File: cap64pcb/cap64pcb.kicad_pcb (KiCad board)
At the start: 2 copper layers, 96 x 8 mm, 29 parts, among them J1 SM05B_SURS_TF, Q1 BSS138, Q2 BSS138, U1 MPR121QR2, U2 SPX3819M5-L-3-3

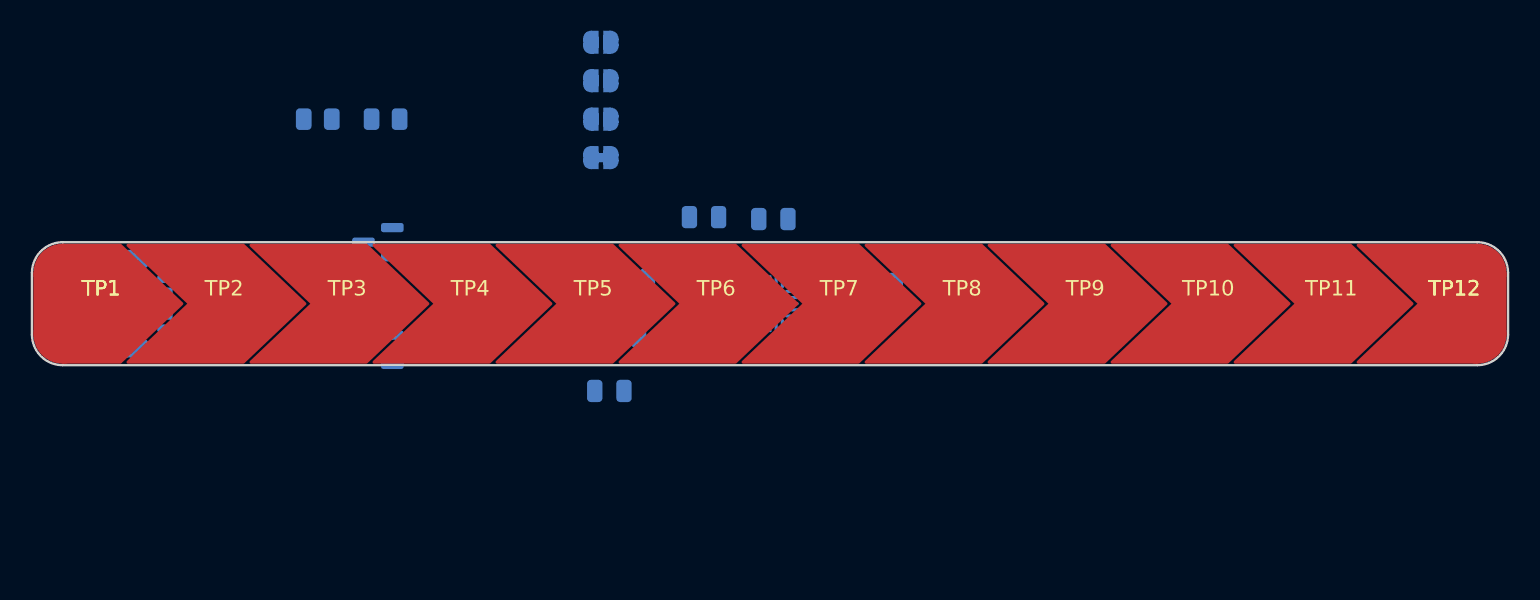
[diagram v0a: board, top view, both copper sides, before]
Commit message: reworked chevrons (merged pads, shrunk to 7.6)
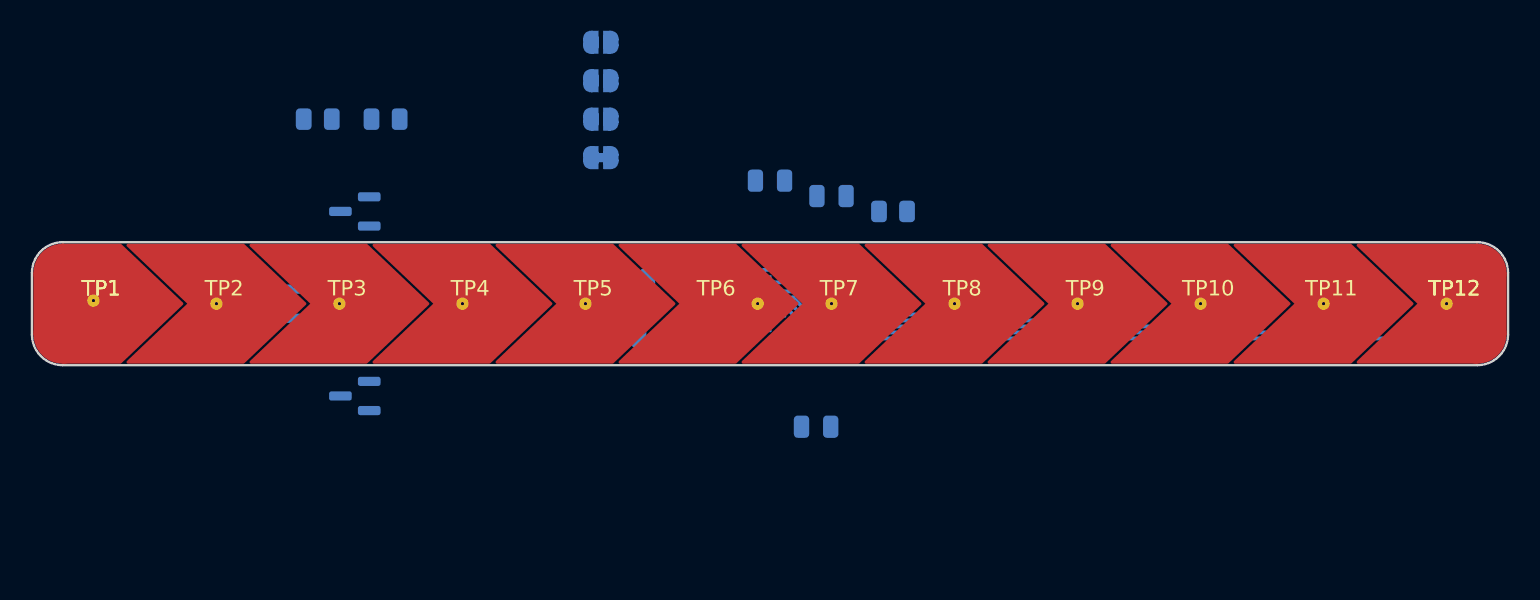
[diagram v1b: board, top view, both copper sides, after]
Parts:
- TP6: footprint cap_pads:CAPPAD_8x8_Chevron_2 -> cap_pads:CAPPAD_8x8_Chevron_2_asym
- moved C5 13.6 mm to (83.0, 53.0)
- moved C2 4.90 mm to (80.0, 37.0)
- moved R1 4.75 mm to (88.0, 39.0)
- moved C1 4.07 mm to (84.0, 38.0)
- moved Q1 3.35 mm to (53.0, 51.0)
- moved U2 3.00 mm to (48.0, 45.0)
- moved Q2 2.50 mm to (53.0, 39.0)
- moved U1 0.80 mm to (79.2, 45.0)
- moved J1 0.50 mm to (40.0, 45.0), turned to -90 degrees
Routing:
- net Net-(U1-Pad19): track 0.00 -> 45.0 mm
- net Net-(U1-Pad18): track 0.00 -> 36.9 mm
- net Net-(U1-Pad17): track 0.00 -> 28.7 mm
- net Net-(U1-Pad16): track 0.00 -> 20.6 mm
- net Net-(U1-Pad15): track 0.00 -> 13.1 mm
- net Net-(U1-Pad14): track 0.00 -> 6.12 mm
- net Net-(U1-Pad13): track 0.00 -> 1.39 mm

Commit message: fixed miniscule spacing error
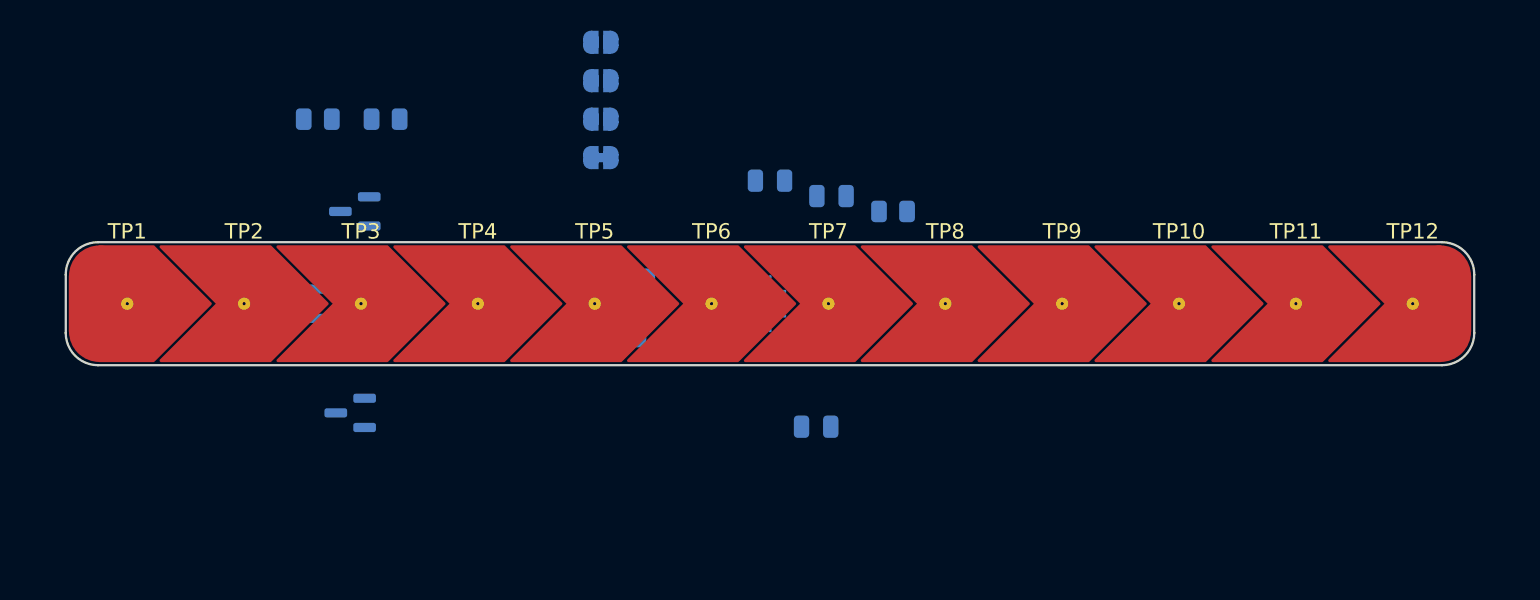
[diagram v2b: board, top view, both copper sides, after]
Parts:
- TP1: footprint cap_pads:CAPPAD_8x8_Chevron_1 -> cap_pads:CAPPAD_7.6x7.6_Chevron_1
- TP10, TP11, TP2, TP3, TP4, TP5, TP7, TP8, TP9: footprint cap_pads:CAPPAD_8x8_Chevron_2 -> cap_pads:CAPPAD_7.6x7.6_Chevron_2
- TP12: footprint cap_pads:CAPPAD_8x8_Chevron_3 -> cap_pads:CAPPAD_7.6x7.6_Chevron_3
- TP6: footprint cap_pads:CAPPAD_8x8_Chevron_2_asym -> cap_pads:CAPPAD_7.6x7.6_Chevron_2
- moved TP1 2.20 mm to (38.2, 45.0)
- moved TP12 2.20 mm to (121.8, 45.0)
- moved J1 2.10 mm to (42.1, 45.0)
- moved TP11 1.80 mm to (114.2, 45.0)
- moved TP2 1.80 mm to (45.8, 45.0)
- moved U2 1.50 mm to (49.5, 45.0)
- moved TP10 1.40 mm to (106.6, 45.0)
- moved TP3 1.40 mm to (53.4, 45.0)
- moved Q1 1.14 mm to (52.7, 52.1)
- moved TP4 1.00 mm to (61.0, 45.0)
- moved TP9 1.00 mm to (99.0, 45.0)
- moved TP5 0.60 mm to (68.6, 45.0)
- moved TP8 0.60 mm to (91.4, 45.0)
- moved TP6 0.20 mm to (76.2, 45.0)
- moved TP7 0.20 mm to (83.8, 45.0)
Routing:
- net Net-(U1-Pad19): track 45.0 -> 0.00 mm
- net Net-(U1-Pad18): track 36.9 -> 0.00 mm
- net Net-(U1-Pad17): track 28.7 -> 0.00 mm
- net Net-(U1-Pad16): track 20.6 -> 0.00 mm
- net Net-(U1-Pad15): track 13.1 -> 0.00 mm
- net Net-(U1-Pad14): track 6.12 -> 0.00 mm
- net Net-(U1-Pad13): track 1.39 -> 0.00 mm
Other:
- board size 96 x 8 mm -> 91.6 x 8 mm

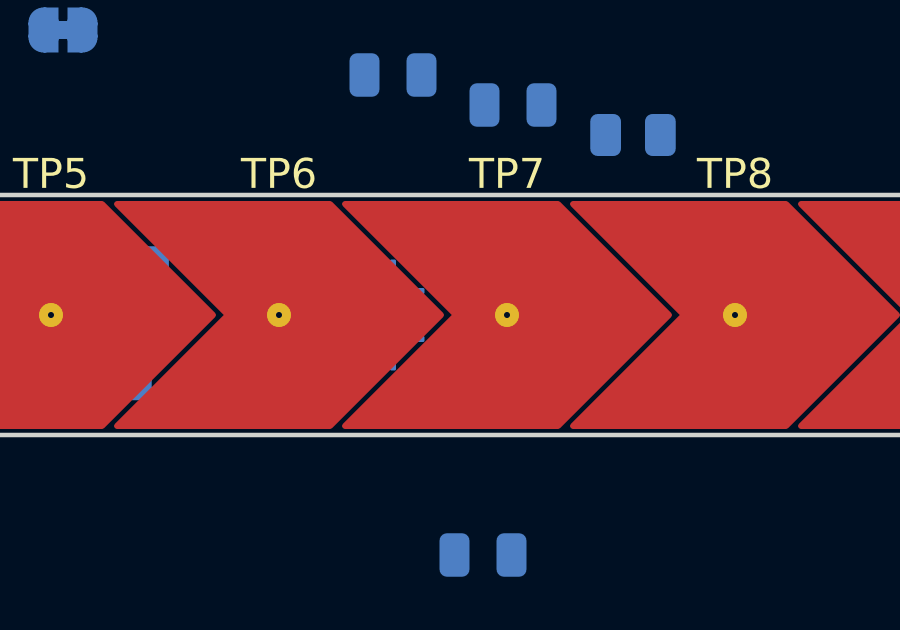
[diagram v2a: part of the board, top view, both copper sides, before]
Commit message: shifted 'via' for center pads
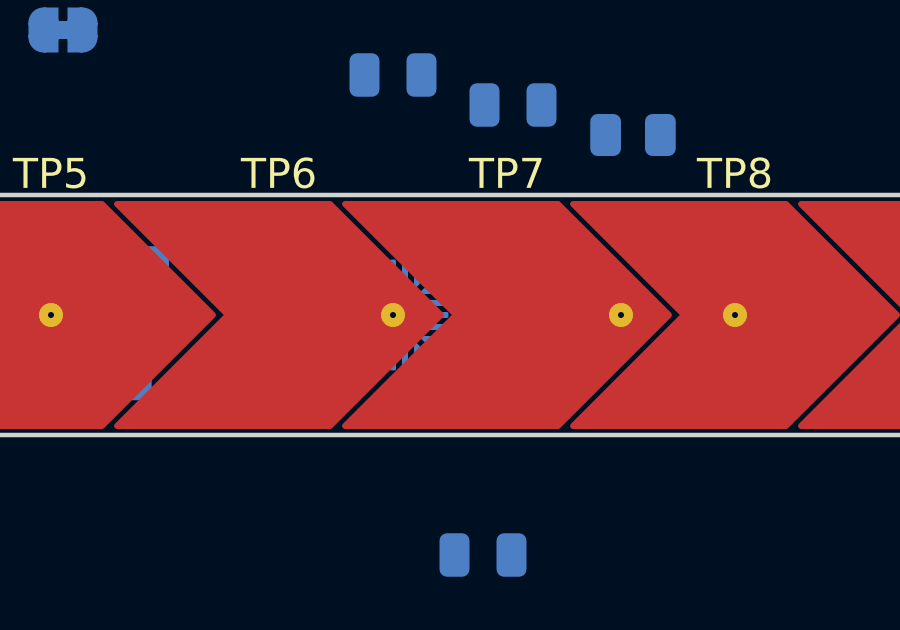
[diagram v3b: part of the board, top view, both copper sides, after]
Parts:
- TP6, TP7: footprint cap_pads:CAPPAD_7.6x7.6_Chevron_2 -> cap_pads:CAPPAD_7.6x7.6_Chevron_2_shifted
- moved U1 0.80 mm to (80.0, 45.0)
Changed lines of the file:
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@@
       (net 23 "Net-(U1-Pad18)") (pinfunction "1") (pintype "passive"))
   )
-  (footprint "cap_pads:CAPPAD_7.6x7.6_Chevron_2" (layer "F.Cu")
+  (footprint "cap_pads:CAPPAD_7.6x7.6_Chevron_2_shifted" (layer "F.Cu")
     (at 83.8 45)
     (property "Sheetfile" "cap64pcb.kicad_sch")
@@
     )
     (fp_rect (start -3.8 -3.8) (end 3.8 3.8) (layer "Dwgs.User") (width 0.1) (fill none))
+    (pad "1" thru_hole circle (at 3.8 0) (size 0.8 0.8) (drill 0.2) (layers *.Cu)
+      (net 19 "Net-(U1-Pad14)") (pinfunction "1") (pintype "passive"))
     (pad "1" smd custom (at 0 0) (size 0.8 0.8) (layers "F.Cu")
       (net 19 "Net-(U1-Pad14)") (pinfunction "1") (pintype "passive")
@@
           ) (width 0.2) (fill yes))
       ))
-    (pad "1" thru_hole circle (at 0 0) (size 0.8 0.8) (drill 0.2) (layers *.Cu)
-      (net 19 "Net-(U1-Pad14)") (pinfunction "1") (pintype "passive"))
   )
   (footprint "cap_pads:CAPPAD_7.6x7.6_Chevron_2" (layer "F.Cu")
@@
       ))
   )
-  (footprint "cap_pads:CAPPAD_7.6x7.6_Chevron_2" (layer "F.Cu")
+  (footprint "cap_pads:CAPPAD_7.6x7.6_Chevron_2_shifted" (layer "F.Cu")
     (at 76.2 45)
     (property "Sheetfile" "cap64pcb.kicad_sch")
@@
           ) (width 0.2) (fill yes))
       ))
-    (pad "1" thru_hole circle (at 0 0) (size 0.8 0.8) (drill 0.2) (layers *.Cu)
+    (pad "1" thru_hole circle (at 3.8 0) (size 0.8 0.8) (drill 0.2) (layers *.Cu)
       (net 18 "Net-(U1-Pad13)") (pinfunction "1") (pintype "passive"))
   )
@@
   )
   (footprint "Package_DFN_QFN:UQFN-20_3x3mm_P0.4mm" (layer "B.Cu")
-    (at 79.2 45 90)
+    (at 80 45 90)
     (descr "UQFN, 20 Pin (https://resurgentsemi.com/wp-content/uploads/2018/09/MPR121_rev5-Resurgent.pdf?d453f8&d453f8), generated with kicad-footprint-generator ipc_noLead_generator.py")
     (tags "UQFN NoLead")

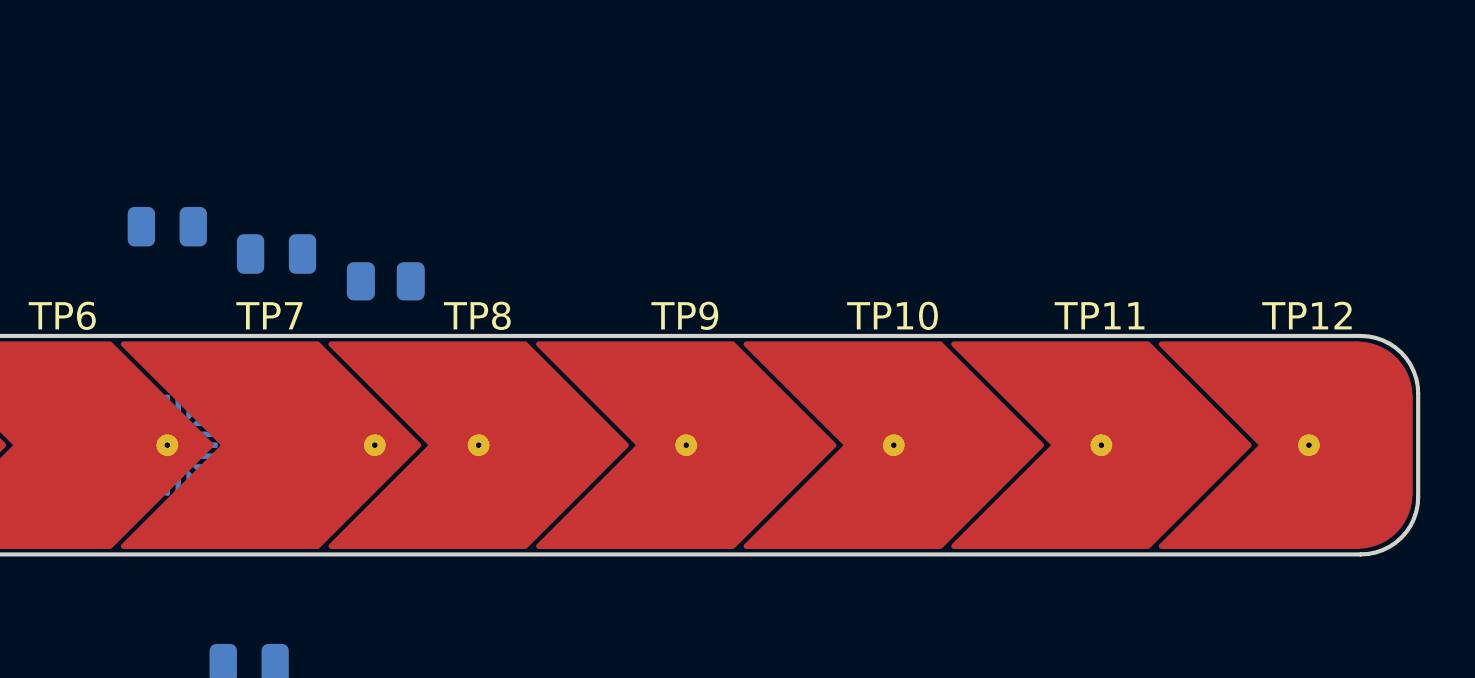
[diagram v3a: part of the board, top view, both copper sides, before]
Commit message: routed pads 7-12
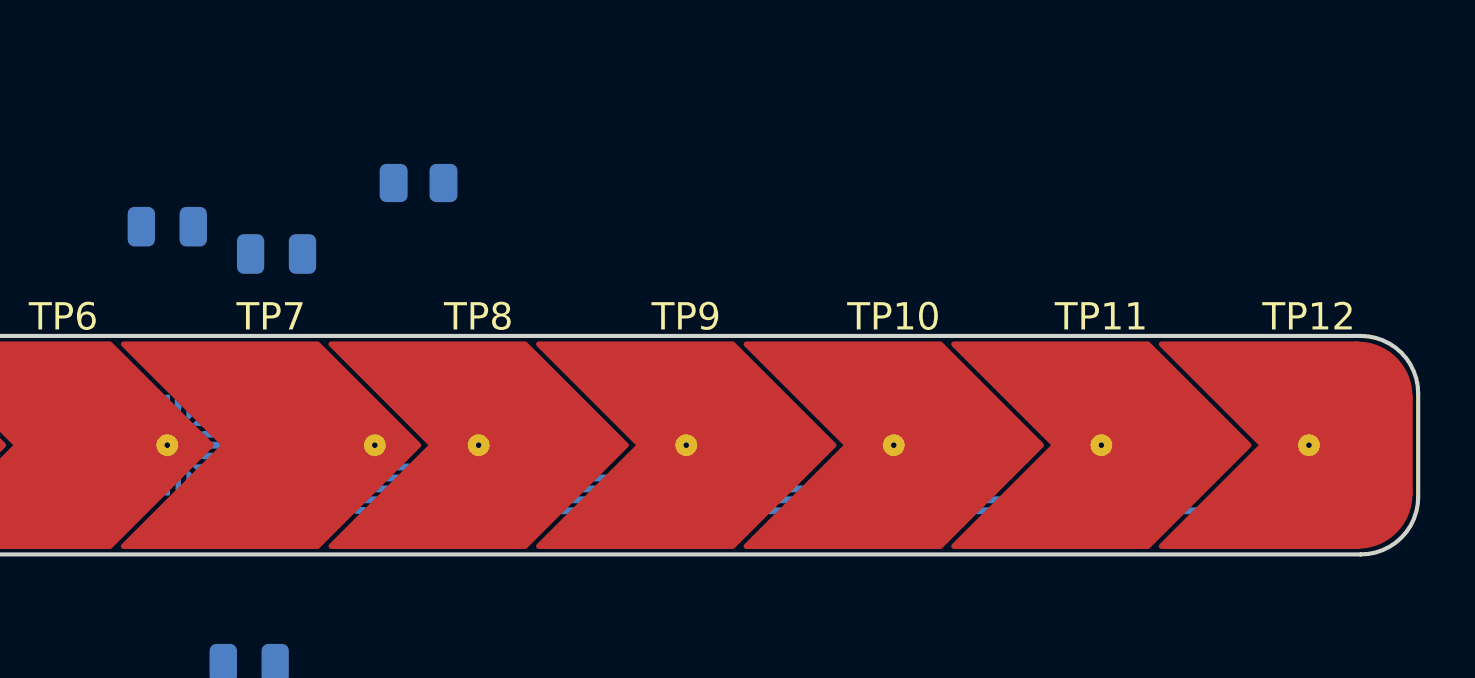
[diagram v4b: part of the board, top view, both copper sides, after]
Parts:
- moved R1 3.79 mm to (89.2, 35.4)
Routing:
- net Net-(U1-Pad19): track 0.00 -> 42.0 mm
- net Net-(U1-Pad18): track 0.00 -> 34.3 mm
- net Net-(U1-Pad17): track 0.00 -> 26.5 mm
- net Net-(U1-Pad16): track 0.00 -> 18.7 mm
- net Net-(U1-Pad15): track 0.00 -> 11.7 mm
- net Net-(U1-Pad14): track 0.00 -> 8.60 mm
- net Net-(U1-Pad13): track 0.00 -> 1.39 mm
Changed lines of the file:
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@@
   )
   (footprint "Resistor_SMD:R_0805_2012Metric" (layer "B.Cu")
-    (at 88 39 180)
+    (at 89.2 35.4 180)
     (descr "Resistor SMD 0805 (2012 Metric), square (rectangular) end terminal, IPC_7351 nominal, (Body size source: IPC-SM-782 page 72, https://www.pcb-3d.com/wordpress/wp-content/uploads/ipc-sm-782a_amendment_1_and_2.pdf), generated with kicad-footprint-generator")
     (tags "resistor")
@@
     (property "Sheetname" "")
     (attr smd)
-    (fp_text reference "R1" (at 0 1.65) (layer "B.SilkS")
-      (effects (font (size 1 1) (thickness 0.15)) (justify mirror))
-    )
-    (fp_text value "75kΩ" (at 0 -1.65) (layer "B.Fab")
+    (fp_text reference "R1" (at 0 1.65) (layer "B.Fab")
+      (effects (font (size 1 1) (thickness 0.15)) (justify mirror))
+    )
+    (fp_text value "75kΩ" (at 0 -1.65) (layer "B.SilkS")
       (effects (font (size 1 1) (thickness 0.15)) (justify mirror))
     )
@@
   (gr_line (start 36.3 41) (end 123.7 41) (layer "Edge.Cuts") (width 0.15))
   (gr_line (start 125.8 46.9) (end 125.8 43.1) (layer "Edge.Cuts") (width 0.15))
+  (segment (start 80 45) (end 80 43.6125) (width 0.25) (layer "B.Cu") (net 18))
+  (segment (start 86.765685 44.765685) (end 85.385786 43.385786) (width 0.25) (layer "B.Cu") (net 19))
+  (segment (start 80.4 43.2) (end 80.4 43.6125) (width 0.25) (layer "B.Cu") (net 19))
+  (segment (start 83.971573 42.8) (end 80.8 42.8) (width 0.25) (layer "B.Cu") (net 19))
+  (segment (start 87.6 45) (end 87.331371 45) (width 0.25) (layer "B.Cu") (net 19))
+  (arc (start 85.385786 43.385786) (mid 84.73694 42.952241) (end 83.971573 42.8) (width 0.25) (layer "B.Cu") (net 19))
+  (arc (start 86.765685 44.765685) (mid 87.025224 44.939104) (end 87.331371 45) (width 0.25) (layer "B.Cu") (net 19))
+  (arc (start 80.4 43.2) (mid 80.517157 42.917157) (end 80.8 42.8) (width 0.25) (layer "B.Cu") (net 19))
+  (segment (start 84.266916 43.6125) (end 80.8 43.6125) (width 0.25) (layer "B.Cu") (net 20))
+  (segment (start 90.185786 45.8) (end 87.614214 45.8) (width 0.25) (layer "B.Cu") (net 20))
+  (segment (start 91.4 45) (end 90.892893 45.507107) (width 0.25) (layer "B.Cu") (net 20))
+  (segment (start 86.907107 45.507107) (end 85.539708 44.139708) (width 0.25) (layer "B.Cu") (net 20))
+  (arc (start 90.892893 45.507107) (mid 90.56847 45.72388) (end 90.185786 45.8) (width 0.25) (layer "B.Cu") (net 20))
+  (arc (start 84.266916 43.6125) (mid 84.955746 43.749517) (end 85.539708 44.139708) (width 0.25) (layer "B.Cu") (net 20))
+  (arc (start 87.614214 45.8) (mid 87.231531 45.72388) (end 86.907107 45.507107) (width 0.25) (layer "B.Cu") (net 20))
+  (segment (start 97.302944 46.2) (end 87.497056 46.2) (width 0.25) (layer "B.Cu") (net 21))
+  (segment (start 99 45) (end 98.151472 45.848528) (width 0.25) (layer "B.Cu") (net 21))
+  (segment (start 84.337258 44.2) (end 81.3875 44.2) (width 0.25) (layer "B.Cu") (net 21))
+  (segment (start 86.648528 45.848528) (end 85.468629 44.668629) (width 0.25) (layer "B.Cu") (net 21))
+  (arc (start 98.151472 45.848528) (mid 97.762164 46.108655) (end 97.302944 46.2) (width 0.25) (layer "B.Cu") (net 21))
+  (arc (start 85.468629 44.668629) (mid 84.949552 44.321793) (end 84.337258 44.2) (width 0.25) (layer "B.Cu") (net 21))
+  (arc (start 87.497056 46.2) (mid 87.037836 46.108655) (end 86.648528 45.848528) (width 0.25) (layer "B.Cu") (net 21))
+  (segment (start 104.420101 46.6) (end 87.391751 46.6) (width 0.25) (layer "B.Cu") (net 22))
+  (segment (start 86.401801 46.189949) (end 85.221902 45.01005) (width 0.25) (layer "B.Cu") (net 22))
+  (segment (start 106.6 45) (end 105.41005 46.18995) (width 0.25) (layer "B.Cu") (net 22))
+  (segment (start 84.231953 44.6) (end 81.3875 44.6) (width 0.25) (layer "B.Cu") (net 22))
+  (arc (start 104.420101 46.6) (mid 104.955857 46.493431) (end 105.41005 46.18995) (width 0.25) (layer "B.Cu") (net 22))
+  (arc (start 87.391751 46.6) (mid 86.855994 46.493431) (end 86.401801 46.189949) (width 0.25) (layer "B.Cu") (net 22))
+  (arc (start 85.221902 45.01005) (mid 84.767709 44.706569) (end 84.231953 44.6) (width 0.25) (layer "B.Cu") (net 22))
+  (segment (start 84.102944 45) (end 81.3875 45) (width 0.25) (layer "B.Cu") (net 23))
+  (segment (start 86.131371 46.531371) (end 84.951472 45.351472) (width 0.25) (layer "B.Cu") (net 23))
+  (segment (start 111.537258 47) (end 87.262742 47) (width 0.25) (layer "B.Cu") (net 23))
+  (segment (start 114.2 45) (end 112.668629 46.531371) (width 0.25) (layer "B.Cu") (net 23))
+  (arc (start 86.131371 46.531371) (mid 86.650448 46.878207) (end 87.262742 47) (width 0.25) (layer "B.Cu") (net 23))
+  (arc (start 84.951472 45.351472) (mid 84.562164 45.091345) (end 84.102944 45) (width 0.25) (layer "B.Cu") (net 23))
+  (arc (start 112.668629 46.531371) (mid 112.149552 46.878207) (end 111.537258 47) (width 0.25) (layer "B.Cu") (net 23))
+  (segment (start 85.872792 46.872792) (end 84.692893 45.692893) (width 0.25) (layer "B.Cu") (net 24))
+  (segment (start 118.654416 47.4) (end 87.145584 47.4) (width 0.25) (layer "B.Cu") (net 24))
+  (segment (start 83.985786 45.4) (end 81.3875 45.4) (width 0.25) (layer "B.Cu") (net 24))
+  (segment (start 121.8 45) (end 119.927208 46.872792) (width 0.25) (layer "B.Cu") (net 24))
+  (arc (start 87.145584 47.4) (mid 86.456754 47.262983) (end 85.872792 46.872792) (width 0.25) (layer "B.Cu") (net 24))
+  (arc (start 83.985786 45.4) (mid 84.368469 45.47612) (end 84.692893 45.692893) (width 0.25) (layer "B.Cu") (net 24))
+  (arc (start 118.654416 47.4) (mid 119.343246 47.262983) (end 119.927208 46.872792) (width 0.25) (layer "B.Cu") (net 24))
 )

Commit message: rough 1-6 routing
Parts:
- moved J1 41.0 mm to (80.0, 60.6), turned to 0 degrees
- moved C3 13.6 mm to (77.6, 30.6)
- moved U2 8.44 mm to (46.8, 37.0)
- moved C4 7.59 mm to (78.6, 51.5)
- moved C1 5.61 mm to (83.7, 32.4)
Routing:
- net Net-(U1-Pad8): track 0.00 -> 41.9 mm
- net Net-(U1-Pad9): track 0.00 -> 34.1 mm
- net Net-(U1-Pad10): track 0.00 -> 26.4 mm
- net Net-(U1-Pad11): track 0.00 -> 19.3 mm
- net Net-(U1-Pad12): track 0.00 -> 12.4 mm
